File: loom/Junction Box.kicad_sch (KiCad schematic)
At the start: 20 parts, among them J18 Power, J26 Shutdown, J27 Faults, J28 LEDs, J29 Status, J30 Reset, J33 Power, J34 Auxillary Contacts, J35 Intended States, J36 TSAL LED Signal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

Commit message: fix(Loom): changed names of netlists
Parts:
- added NT8: GROUND POINT, symbol Device:NetTie_4
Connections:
- net +AIR.Intended.On renamed +AIR.INTENDED.ON
- net -AIR.Intended.On renamed -AIR.INTENDED.ON
- net BMS.Fault renamed BMS.FAULT
- net BMS.Fault.Latched.LED renamed BMS.FAULT.LATCHED.LED
- net BMS.Fault.Latched.Status renamed BMS.FAULT.LATCHED.STATUS
- net Datalogger.FSUK.HV+ renamed DATALOGGER.FSUK.HV+
- net Datalogger.FSUK.HV- renamed DATALOGGER.FSUK.HV-
- net Discharge.GND renamed DISCHARGE.GND
- net DISCHARGE.GND: now also NT8.2
- net Discharge.HV+ renamed DISCHARGE.HV+
- net Discharge.HV- renamed DISCHARGE.HV-
- net Discharge.Resistor.In.HV- renamed DISCHARGE.RESISTOR.IN.HV-
- net Green.LED.On.Dash renamed GREEN.LED.ON.DASH
- net Green.LED.On.TSAL renamed GREEN.LED.ON.TSAL
- net HV.TSMP+.Resistor.In renamed HV.TSMP+.RESISTOR.IN
- net HV_Sense.HV+ renamed HV_SENSE.HV+
- net HV_Sense.HV- renamed HV_SENSE.HV-
- net HvS.EXC renamed HVS.EXC
- net HvS.GND renamed HVS.GND
- net IMD.Fault.Latched.LED renamed IMD.FAULT.LATCHED.LED
- net IMD.Fault.Latched.Status renamed IMD.FAULT.LATCHED.STATUS
- net Latch.EXC renamed LATCHING.EXC
- net Latch.GND renamed LATCHING.GND
- net LATCHING.GND: now also NT8.3
- net Neg_AIR.AUX.EXC renamed NEG_AIR.AUX.EXC
- net Neg_AIR.AUX.GND renamed NEG_AIR.AUX.GND
- net Pos_AIR.AUX.EXC renamed POS_AIR.AUX.EXC
- net Pos_AIR.AUX.GND renamed POS_AIR.AUX.GND
- net Precharge.Intended.On renamed PRECHARGE.INTENDED.ON
- net Red.LED.On.Dash renamed RED.LED.ON.DASH
- net Red.LED.On.TSAL renamed RED.LED.ON.TSAL
- net Reset.Switch.SIG1 renamed RESET.SWITCH.SIG1
- net Reset.Switch.SIG2 renamed RESET.SWITCH.SIG2
- net SHUT.Discharge renamed SHUT.DISCHARGE
- net TSMP.Resistor.In.HV+ renamed TSMP.RESISTOR.IN.HV+
- net TSMP.Resistor.In.HV- renamed TSMP.RESISTOR.IN.HV-
- net TSMP.RESISTOR.IN.HV-: no longer TSMP-.Resistor.2
- new net JUNCTION.BOX.GND: NT8.4
- new net TSMP.RESISTOR.In.HV-: TSMP-.Resistor.2
- no-connect marks 5 -> 8

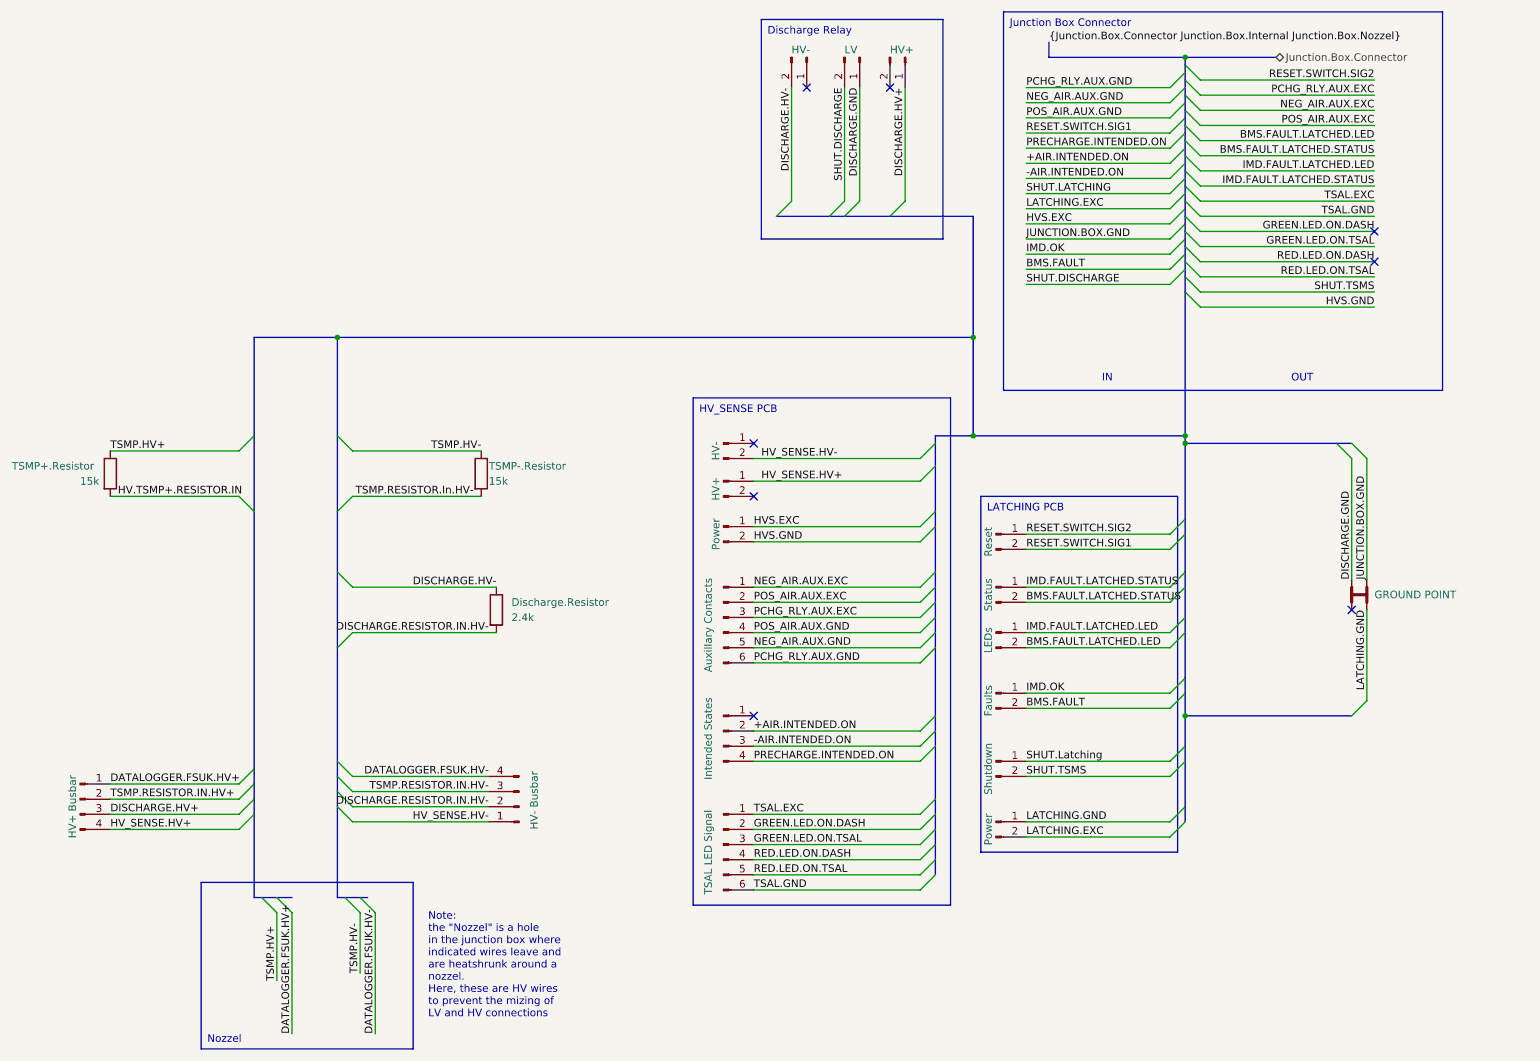
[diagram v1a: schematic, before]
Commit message: feat(Loom): Updated version of Loom Schematic
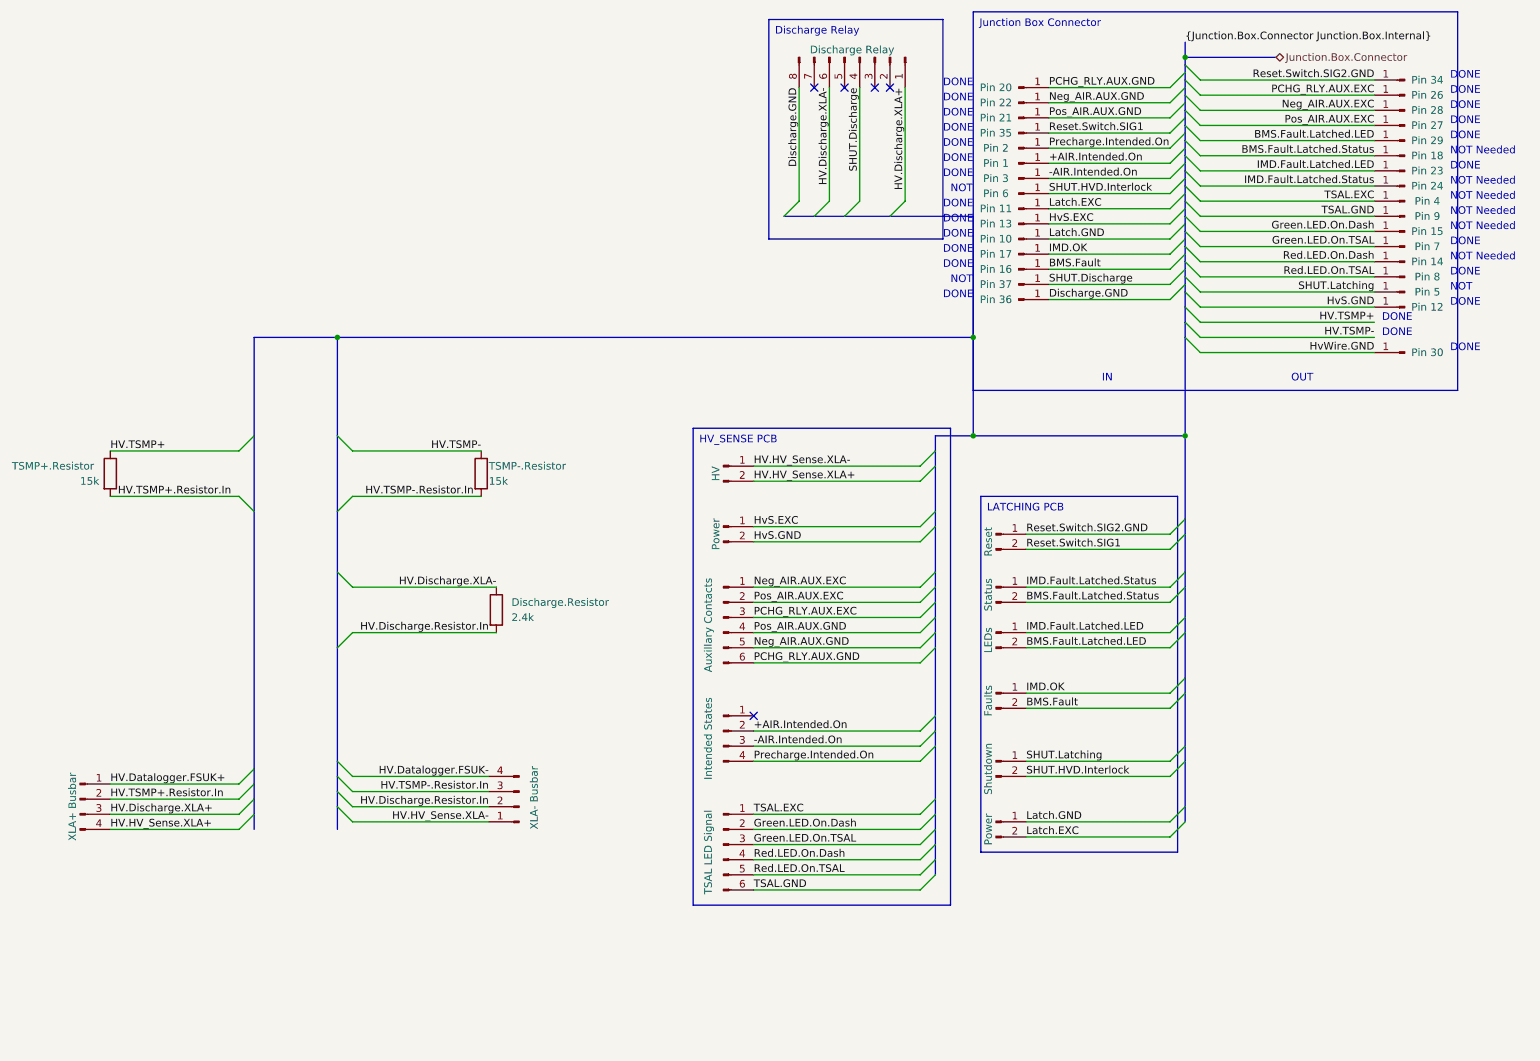
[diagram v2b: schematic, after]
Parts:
- removed J38: HV+, symbol Connector:Conn_01x02_Pin
- removed J89: LV, symbol Connector:Conn_01x02_Pin
- removed J90, J91: HV-, symbol Connector:Conn_01x02_Pin
- removed NT8: GROUND POINT, symbol Device:NetTie_4
- added J100: Pin 17, symbol Connector:Conn_01x01_Pin
- added J143: Pin 9, symbol Connector:Conn_01x01_Pin
- added J144: Pin 15, symbol Connector:Conn_01x01_Pin
- added J145: Pin 7, symbol Connector:Conn_01x01_Pin
- added J146: Pin 14, symbol Connector:Conn_01x01_Pin
- added J147: Pin 8, symbol Connector:Conn_01x01_Pin
- added J148: Pin 13, symbol Connector:Conn_01x01_Pin
- added J149: Pin 12, symbol Connector:Conn_01x01_Pin
- added J150: Pin 2, symbol Connector:Conn_01x01_Pin
- added J151: Pin 1, symbol Connector:Conn_01x01_Pin
- added J152: Pin 3, symbol Connector:Conn_01x01_Pin
- added J153: Pin 28, symbol Connector:Conn_01x01_Pin
- added J154: Pin 22, symbol Connector:Conn_01x01_Pin
- added J155: Pin 27, symbol Connector:Conn_01x01_Pin
- added J156: Pin 21, symbol Connector:Conn_01x01_Pin
- added J157: Pin 26, symbol Connector:Conn_01x01_Pin
- added J158: Pin 20, symbol Connector:Conn_01x01_Pin
- added J159: Pin 37, symbol Connector:Conn_01x01_Pin
- added J160: Pin 36, symbol Connector:Conn_01x01_Pin
- added J179: Pin 30, symbol Connector:Conn_01x01_Pin
- added J38: Discharge Relay, symbol Connector:Conn_01x08_Pin
- added J51: Pin 4, symbol Connector:Conn_01x01_Pin
- added J89: Pin 11, symbol Connector:Conn_01x01_Pin
- added J90: Pin 10, symbol Connector:Conn_01x01_Pin
- added J91: Pin 6, symbol Connector:Conn_01x01_Pin
- added J92: Pin 5, symbol Connector:Conn_01x01_Pin
- added J93: Pin 34, symbol Connector:Conn_01x01_Pin
- added J94: Pin 35, symbol Connector:Conn_01x01_Pin
- added J95: Pin 18, symbol Connector:Conn_01x01_Pin
- added J96: Pin 24, symbol Connector:Conn_01x01_Pin
- added J97: Pin 29, symbol Connector:Conn_01x01_Pin
- added J98: Pin 23, symbol Connector:Conn_01x01_Pin
- added J99: Pin 16, symbol Connector:Conn_01x01_Pin
- J37: value HV+ -> HV
- J39: value HV+ Busbar -> XLA+ Busbar
- J40: value HV- Busbar -> XLA- Busbar
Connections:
- net HV_SENSE.HV- is gone; now on net HV.HV_Sense.XLA-: J40.1 (Pin_1)
- net TSMP.RESISTOR.IN.HV+ is gone; now on net HV.TSMP+.Resistor.In: J39.2 (Pin_2)
- net TSMP.RESISTOR.In.HV- is gone; now on net HV.TSMP-.Resistor.In: TSMP-.Resistor.2
- net IMD.OK: now also J100.1 (Pin_1)
- net PCHG_RLY.AUX.EXC: now also J157.1 (Pin_1)
- net PCHG_RLY.AUX.GND: now also J158.1 (Pin_1)
- net SHUT.Latching: now also J92.1 (Pin_1)
- net TSAL.EXC: now also J51.1 (Pin_1)
- net TSAL.GND: now also J143.1 (Pin_1)
- net HV.HV_Sense.XLA+: now reaches J37.2 (Pin_2)
- net HV.HV_Sense.XLA+: now also J39.4 (Pin_4)
- net +AIR.INTENDED.ON renamed +AIR.Intended.On
- net +AIR.Intended.On: now also J151.1 (Pin_1)
- net -AIR.INTENDED.ON renamed -AIR.Intended.On
- net -AIR.Intended.On: now also J152.1 (Pin_1)
- net BMS.FAULT renamed BMS.Fault
- net BMS.Fault: now also J99.1 (Pin_1)
- net BMS.FAULT.LATCHED.LED renamed BMS.Fault.Latched.LED
- net BMS.Fault.Latched.LED: now also J97.1 (Pin_1)
- net BMS.FAULT.LATCHED.STATUS renamed BMS.Fault.Latched.Status
- net BMS.Fault.Latched.Status: now also J95.1 (Pin_1)
- net DATALOGGER.FSUK.HV+ renamed HV.Datalogger.FSUK+
- net DATALOGGER.FSUK.HV- renamed HV.Datalogger.FSUK-
- net DISCHARGE.HV+ renamed HV.Discharge.XLA+
- net HV.Discharge.XLA+: now also J38.1 (Pin_1)
- net DISCHARGE.HV- renamed HV.Discharge.XLA-
- net HV.Discharge.XLA-: now also J38.6 (Pin_6)
- net DISCHARGE.RESISTOR.IN.HV- renamed HV.Discharge.Resistor.In
- net GREEN.LED.ON.DASH renamed Green.LED.On.Dash
- net Green.LED.On.Dash: now also J144.1 (Pin_1)
- net GREEN.LED.ON.TSAL renamed Green.LED.On.TSAL
- net Green.LED.On.TSAL: now also J145.1 (Pin_1)
- net HV.TSMP+.RESISTOR.IN renamed HV.TSMP+.Resistor.In
- net HVS.EXC renamed HvS.EXC
- net HvS.EXC: now also J148.1 (Pin_1)
- net HVS.GND renamed HvS.GND
- net HvS.GND: now also J149.1 (Pin_1)
- net HV_SENSE.HV+ renamed HV.HV_Sense.XLA-
- net HV.HV_Sense.XLA-: no longer J39.4 (Pin_4)
- net IMD.FAULT.LATCHED.LED renamed IMD.Fault.Latched.LED
- net IMD.Fault.Latched.LED: now also J98.1 (Pin_1)
- net IMD.FAULT.LATCHED.STATUS renamed IMD.Fault.Latched.Status
- net IMD.Fault.Latched.Status: now also J96.1 (Pin_1)
- net LATCHING.EXC renamed Latch.EXC
- net Latch.EXC: now also J89.1 (Pin_1)
- net LATCHING.GND renamed Latch.GND
- net Latch.GND: now also J90.1 (Pin_1)
- net NEG_AIR.AUX.EXC renamed Neg_AIR.AUX.EXC
- net Neg_AIR.AUX.EXC: now also J153.1 (Pin_1)
- net NEG_AIR.AUX.GND renamed Neg_AIR.AUX.GND
- net Neg_AIR.AUX.GND: now also J154.1 (Pin_1)
- net POS_AIR.AUX.EXC renamed Pos_AIR.AUX.EXC
- net Pos_AIR.AUX.EXC: now also J155.1 (Pin_1)
- net POS_AIR.AUX.GND renamed Pos_AIR.AUX.GND
- net Pos_AIR.AUX.GND: now also J156.1 (Pin_1)
- net PRECHARGE.INTENDED.ON renamed Precharge.Intended.On
- net Precharge.Intended.On: now also J150.1 (Pin_1)
- net RED.LED.ON.DASH renamed Red.LED.On.Dash
- net Red.LED.On.Dash: now also J146.1 (Pin_1)
- net RED.LED.ON.TSAL renamed Red.LED.On.TSAL
- net Red.LED.On.TSAL: now also J147.1 (Pin_1)
- net RESET.SWITCH.SIG1 renamed Reset.Switch.SIG1
- net Reset.Switch.SIG1: now also J94.1 (Pin_1)
- net RESET.SWITCH.SIG2 renamed Reset.Switch.SIG2.GND
- net Reset.Switch.SIG2.GND: now also J93.1 (Pin_1)
- net SHUT.TSMS renamed SHUT.HVD.Interlock
- net SHUT.HVD.Interlock: now also J91.1 (Pin_1)
- net TSMP.HV+ renamed HV.TSMP+
- net TSMP.HV- renamed HV.TSMP-
- net TSMP.RESISTOR.IN.HV- renamed HV.TSMP-.Resistor.In
- new net Discharge.GND: J160.1 (Pin_1), J38.8 (Pin_8)
- new net HvWire.GND: J179.1 (Pin_1)
- new net SHUT.Discharge: J159.1 (Pin_1), J38.4 (Pin_4)
- no-connect marks 8 -> 5
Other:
- note added: "DONE"
- note added: "NOT"
- note added: "NOT Needed"
- note removed: "Note: the "Nozzel" is a hole in the junction box where indicated wires leave and are heatshrunk around a nozzel. Here, these are HV wires to prevent the mizing of LV and HV connections"
